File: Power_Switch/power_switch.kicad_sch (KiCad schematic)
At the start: 3 parts, among them J1 Conn_01x02_Pin, J2 Conn_01x02_Socket, SW1 SW_SPDT

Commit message: small changes - probably wont use
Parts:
- added H1, H2, H3: MountingHole, MountingHole:MountingHole_2.7mm_M2.5, symbol Mechanical:MountingHole
- added TP1, TP2: TestPoint, TestPoint:TestPoint_Pad_D1.5mm, symbol Connector:TestPoint
- J1, J2: footprint Connector_JST:JST_SH_BM02B-SRSS-TB_1x02-1MP_P1.00mm_Vertical -> Connector_JST:JST_SH_SM02B-SRSS-TB_1x02-1MP_P1.00mm_Horizontal
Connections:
- net V_BAT_SWITCHED: now reaches SW1.1 (A)
- net V_BAT_SWITCHED: now also J2.1 (Pin_1)
- net V_BAT: now reaches J1.1 (Pin_1), SW1.2 (B)
- net V_BAT: now also TP1.1
- net at SW1.3 (C): no longer J2.1 (Pin_1)
- net GND: now reaches J1.2 (Pin_2), J2.2 (Pin_2)
- net GND: now also TP2.1

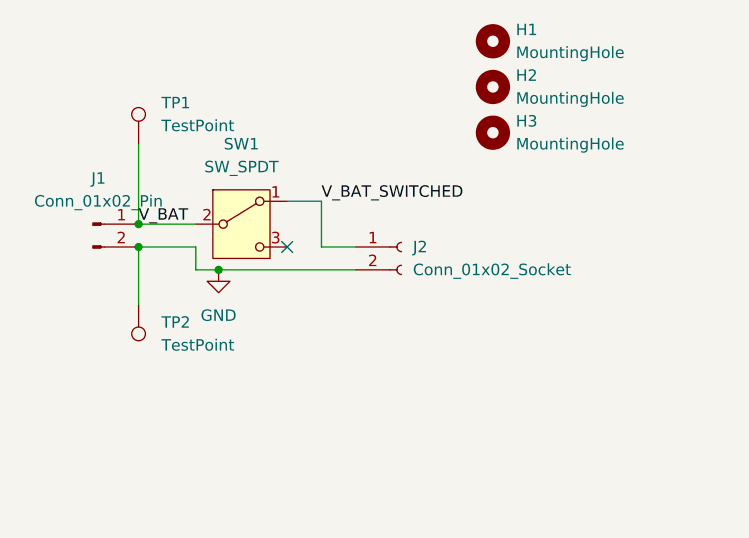
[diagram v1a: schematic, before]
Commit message: Switch_LED_daughter_board done
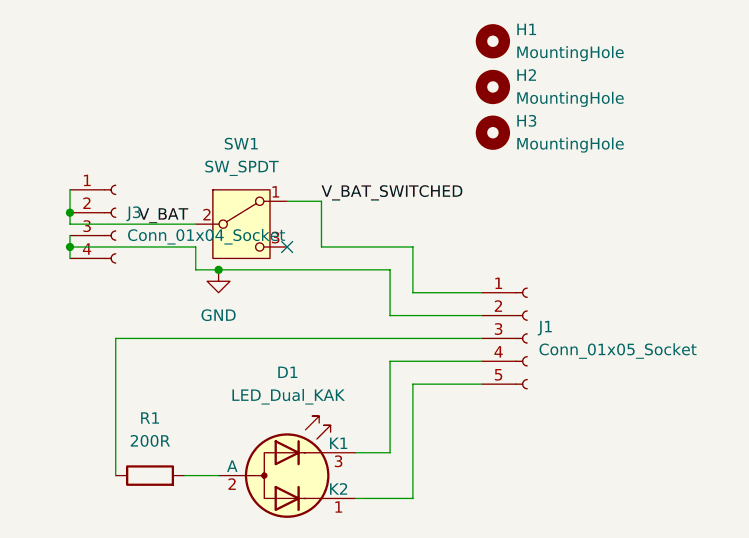
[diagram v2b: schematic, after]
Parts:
- removed J1: Conn_01x02_Pin, Connector_JST:JST_SH_SM02B-SRSS-TB_1x02-1MP_P1.00mm_Horizontal, symbol Connector:Conn_01x02_Pin
- removed J2: Conn_01x02_Socket, Connector_JST:JST_SH_SM02B-SRSS-TB_1x02-1MP_P1.00mm_Horizontal, symbol Connector:Conn_01x02_Socket
- removed TP1, TP2: TestPoint, TestPoint:TestPoint_Pad_D1.5mm, symbol Connector:TestPoint
- added D1: LED_Dual_KAK, JohnDeereLibrary:LED_Wurth_WL-SBSW, symbol Device:LED_Dual_KAK
- added J1: Conn_01x05_Socket, JohnDeereLibrary:5_pad_connector, symbol Connector:Conn_01x05_Socket
- added J3: Conn_01x04_Socket, JohnDeereLibrary:4_pad_connector, symbol Connector:Conn_01x04_Socket
- added R1: 200R, Resistor_SMD:R_0603_1608Metric, symbol Device:R
- SW1: footprint JohnDeereLibrary:ET01M3D1SAPE -> JohnDeereLibrary:ET01MD1CBE
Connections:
- net GND: now also J1.2 (Pin_2), J3.3 (Pin_3), J3.4 (Pin_4)
- net V_BAT: now also J3.1 (Pin_1), J3.2 (Pin_2)
- net V_BAT_SWITCHED: now also J1.1 (Pin_1)
- new net: J1.3 (Pin_3), R1.1
- new net: D1.2 (A), R1.2
- new net: D1.3 (K1), J1.4 (Pin_4)
- new net: D1.1 (K2), J1.5 (Pin_5)

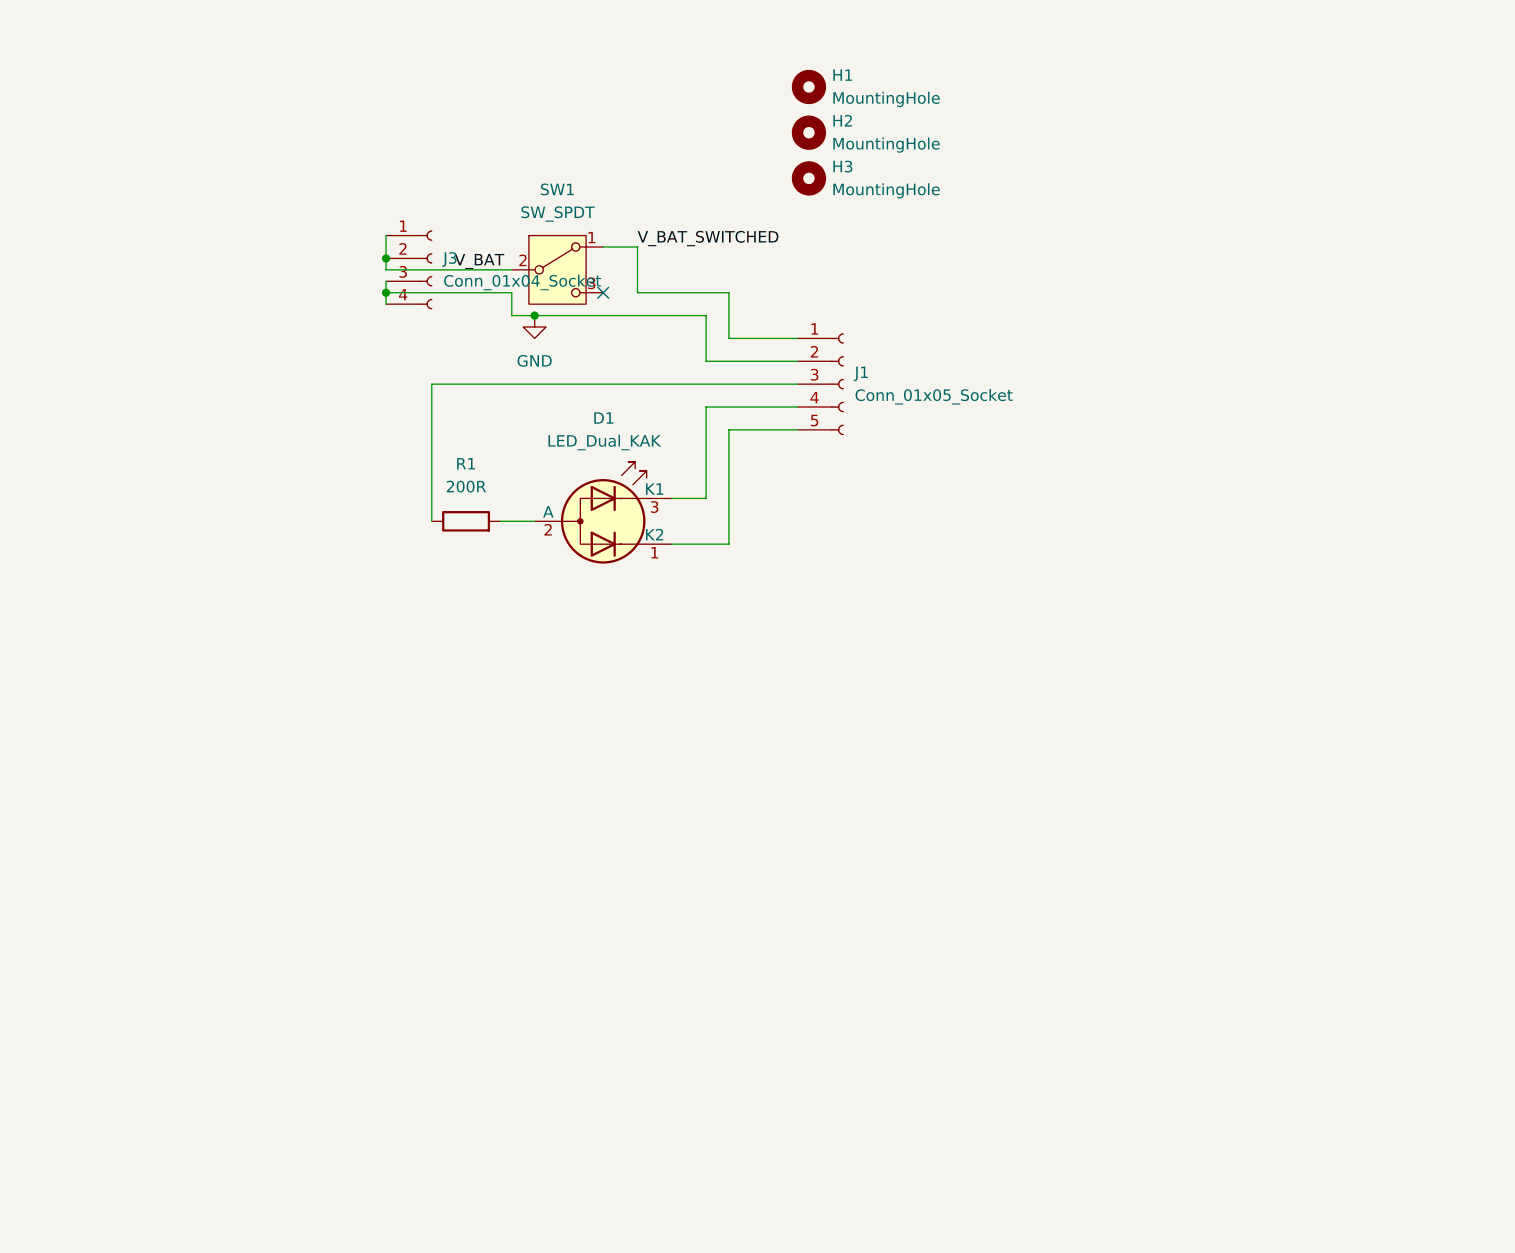
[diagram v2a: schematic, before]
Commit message: small changes to UX for charging
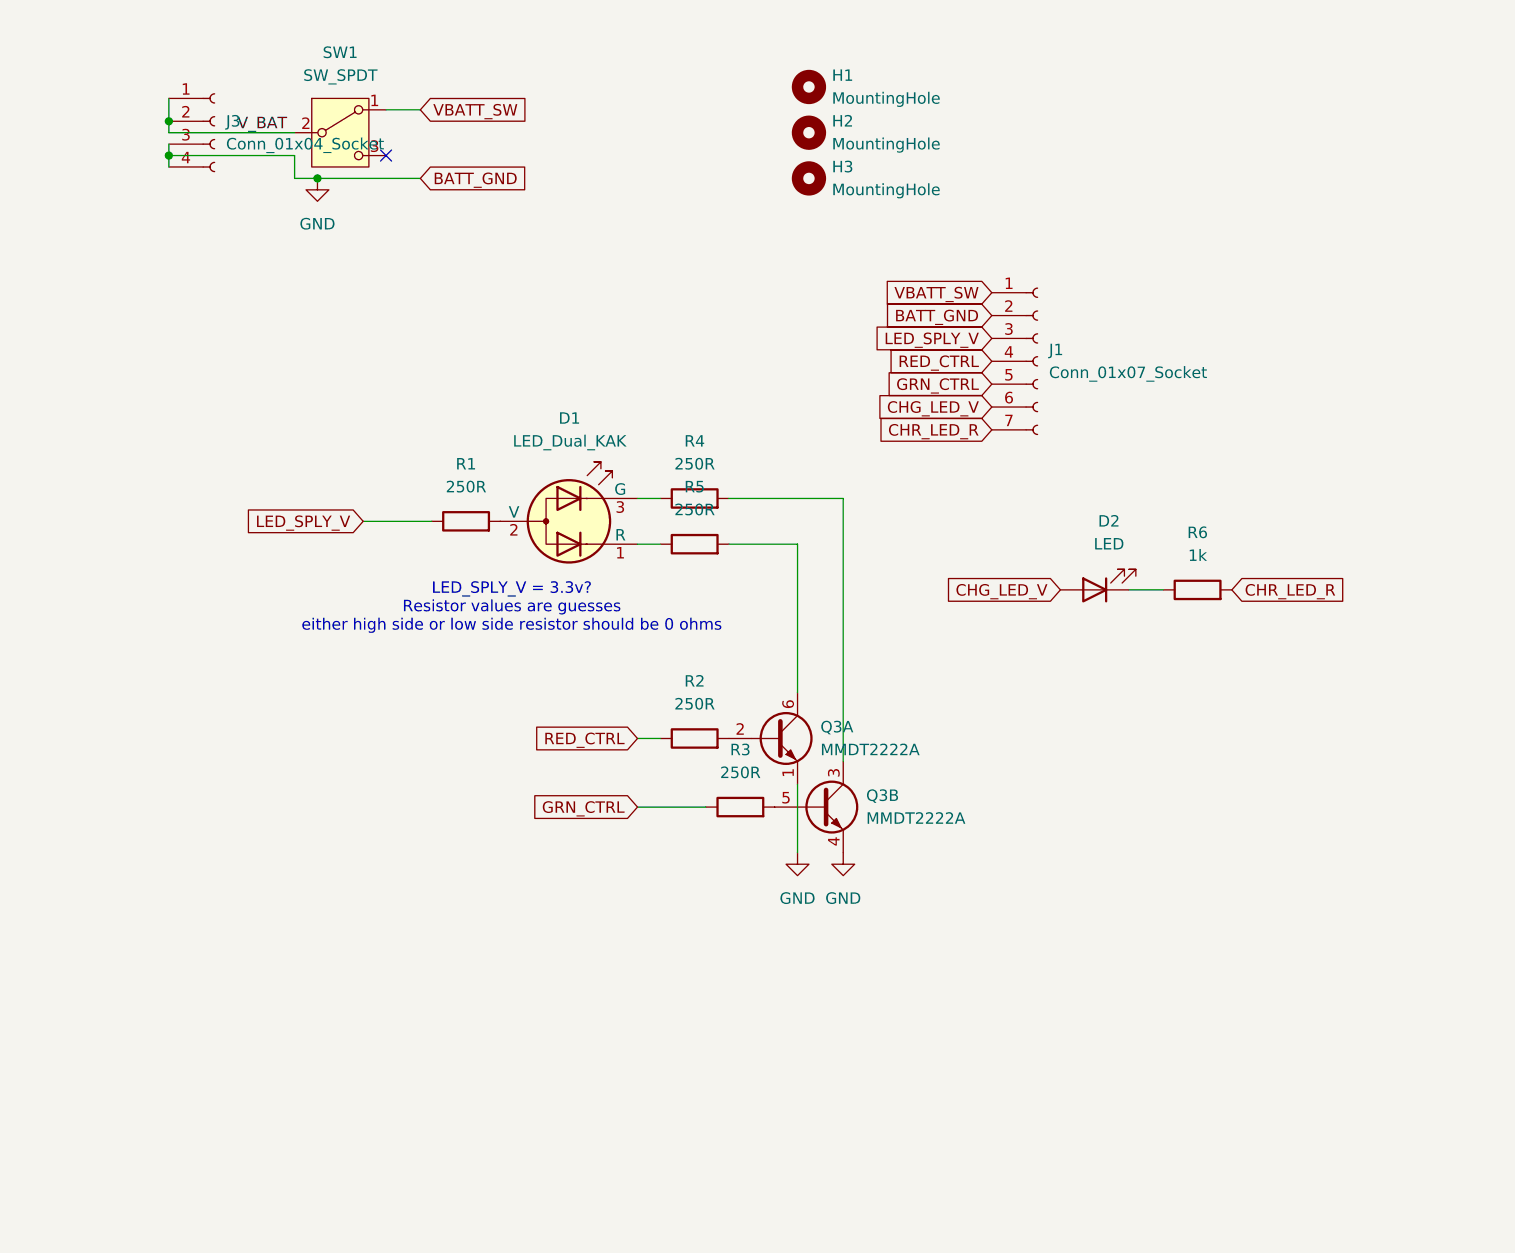
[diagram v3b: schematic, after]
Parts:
- removed J1: Conn_01x05_Socket, JohnDeereLibrary:5_pad_connector, symbol Connector:Conn_01x05_Socket
- added D2: LED, JohnDeereLibrary:LED_WURTH_155060AS75300, symbol Device:LED
- added J1: Conn_01x07_Socket, JohnDeereLibrary:7_pad_connector, symbol Connector:Conn_01x07_Socket
- added Q3: MMDT2222A, Package_TO_SOT_SMD:SOT-363_SC-70-6, symbol Transistor_BJT:MMDT2222A
- added R2, R3, R4, R5: 250R, Resistor_SMD:R_0603_1608Metric, symbol Device:R
- added R6: 1k, Resistor_SMD:R_0603_1608Metric, symbol Device:R
- R1: value 200R -> 250R
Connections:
- net GND: now also J1.2 (Pin_2), Q3.1 (E1), Q3.4 (E2)
- net LED_SPLY_V: now reaches R1.1
- net LED_SPLY_V: now also J1.3 (Pin_3)
- net at D1.3 (G): now also R4.1
- net at D1.1 (R): now also R5.1
- net V_BAT_SWITCHED renamed VBATT_SW
- net VBATT_SW: now also J1.1 (Pin_1)
- new net: Q3.2 (B1), R2.2
- new net: Q3.6 (C1), R5.2
- new net: D2.1 (K), R6.1
- new net: Q3.3 (C2), R4.2
- new net: Q3.5 (B2), R3.2
- new net CHG_LED_V: D2.2 (A), J1.6 (Pin_6)
- new net CHR_LED_R: J1.7 (Pin_7), R6.2
- new net GRN_CTRL: J1.5 (Pin_5), R3.1
- new net RED_CTRL: J1.4 (Pin_4), R2.1
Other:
- note added: "LED_SPLY_V = 3.3v? Resistor values are guesses either high side or low side resistor should be 0 ohms"
- moved on the sheet: D1, J3, SW1

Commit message: Finished Switch PCB - Almost done with Keyboard (Need to fix 3v3 and GND)
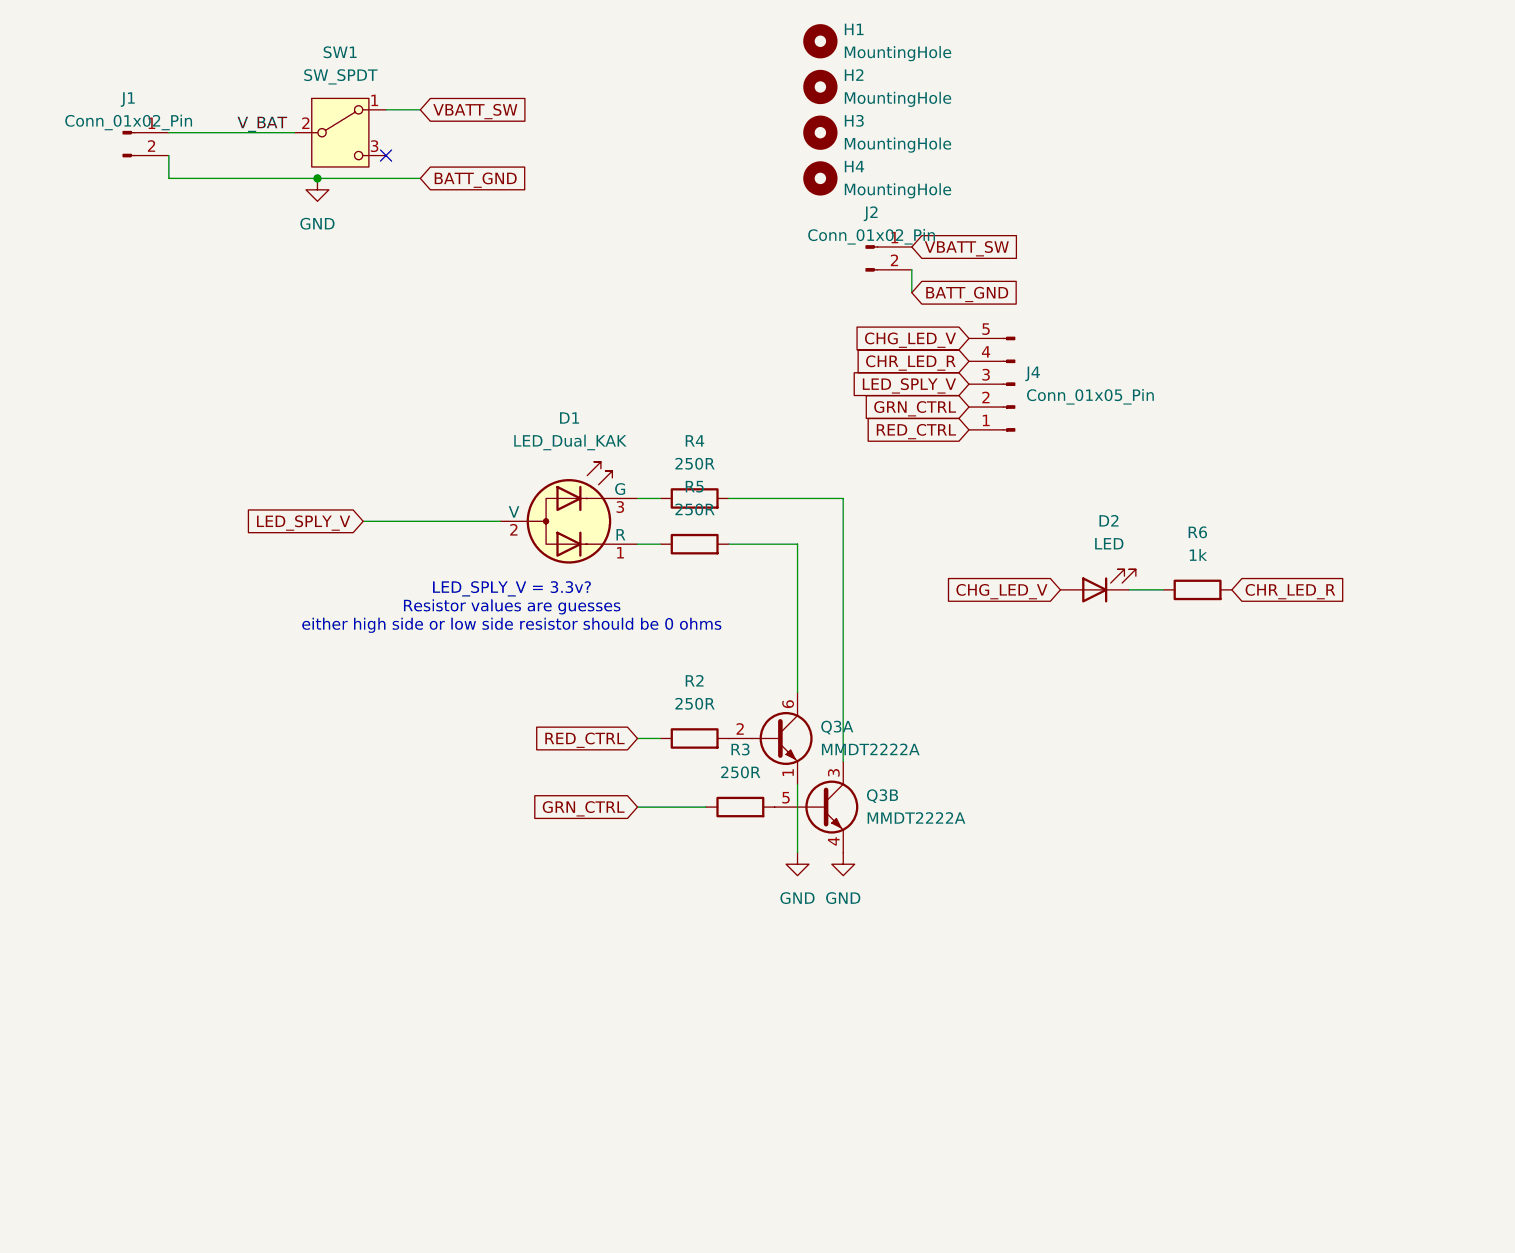
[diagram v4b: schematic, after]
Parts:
- removed J1: Conn_01x07_Socket, JohnDeereLibrary:7_pad_connector, symbol Connector:Conn_01x07_Socket
- removed J3: Conn_01x04_Socket, JohnDeereLibrary:4_pad_connector, symbol Connector:Conn_01x04_Socket
- removed R1: 250R, Resistor_SMD:R_0603_1608Metric, symbol Device:R
- added H4: MountingHole, MountingHole:MountingHole_2.7mm_M2.5, symbol Mechanical:MountingHole
- added J1, J2: Conn_01x02_Pin, JohnDeereLibrary:2_pad_connector, symbol Connector:Conn_01x02_Pin
- added J4: Conn_01x05_Pin, JohnDeereLibrary:5_pad_connector, symbol Connector:Conn_01x05_Pin
- R2, R3, R4, R5, R6: footprint Resistor_SMD:R_0603_1608Metric -> Resistor_SMD:R_0402_1005Metric
- SW1: footprint JohnDeereLibrary:ET01MD1CBE -> JohnDeereLibrary:ET01M3D1SAPE
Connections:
- net CHG_LED_V: now also J4.5 (Pin_5)
- net CHR_LED_R: now also J4.4 (Pin_4)
- net GND: now also J1.2 (Pin_2), J2.2 (Pin_2)
- net GRN_CTRL: now also J4.2 (Pin_2)
- net LED_SPLY_V: now also D1.2 (V), J4.3 (Pin_3)
- net RED_CTRL: now also J4.1 (Pin_1)
- net VBATT_SW: now also J2.1 (Pin_1)
- net V_BAT: now also J1.1 (Pin_1)
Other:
- moved on the sheet: H1, H2, H3

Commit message: small changes to led
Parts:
- removed D1: LED_Dual_KAK, JohnDeereLibrary:LED_Wurth_WL-SBSW, symbol Device:LED_Dual_KAK
- removed D2: LED, JohnDeereLibrary:LED_WURTH_155060AS75300, symbol Device:LED
- removed H3, H4: MountingHole, MountingHole:MountingHole_2.7mm_M2.5, symbol Mechanical:MountingHole
- removed J4: Conn_01x05_Pin, JohnDeereLibrary:5_pad_connector, symbol Connector:Conn_01x05_Pin
- removed Q3: MMDT2222A, Package_TO_SOT_SMD:SOT-363_SC-70-6, symbol Transistor_BJT:MMDT2222A
- removed R2, R3, R4, R5: 250R, Resistor_SMD:R_0402_1005Metric, symbol Device:R
- removed R6: 1k, Resistor_SMD:R_0402_1005Metric, symbol Device:R
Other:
- note removed: "LED_SPLY_V = 3.3v? Resistor values are guesses either high side or low side resistor should be 0 ohms"

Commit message: Power switch done
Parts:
- removed J1, J2: Conn_01x02_Pin, JohnDeereLibrary:2_pad_connector, symbol Connector:Conn_01x02_Pin
- added H3, H4: MountingHole, MountingHole:MountingHole_2.2mm_M2_ISO14580, symbol Mechanical:MountingHole
- added J1: Conn_01x03_Pin, Connector_Molex:Molex_Pico-EZmate_78171-0003_1x03-1MP_P1.20mm_Vertical, symbol Connector:Conn_01x03_Pin
- H1: footprint MountingHole:MountingHole_2.7mm_M2.5 -> MountingHole:MountingHole_2.2mm_M2_ISO14580
- H2: footprint MountingHole:MountingHole_2.7mm_M2.5 -> MountingHole:MountingHole_2.2mm_M2_ISO14580_Pad_TopBottom; symbol Mechanical:MountingHole -> Mechanical:MountingHole_Pad
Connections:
- net GND: now also H2.1, SW1.3 (C), J1.3 (Pin_3)
- net VBATT_SW renamed +BATT
- net +BATT: now also J1.1 (Pin_1)
- net V_BAT: no longer names the net of SW1.2 (B)
- net V_BAT: now also J1.2 (Pin_2)
- no-connect marks 1 -> 0

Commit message: Orginizing and small work done
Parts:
- added C10, C12: 4.7uF, Capacitor_SMD:C_0402_1005Metric, symbol Device:C
- added C11: 1uF, Capacitor_SMD:C_0402_1005Metric, symbol Device:C
- added D85: LED, JohnDeereLibrary:LED_WURTH_155060AS75300, symbol Device:LED
- added J2: FFC2B28-06-G, GCT:GCT_FFC2B28-06-G, symbol FFC2B28-06-G:FFC2B28-06-G
- added J6: Conn_01x02_Pin, Connector_PinSocket_2.54mm:PinSocket_1x02_P2.54mm_Vertical, symbol Connector:Conn_01x02_Pin
- added Q9: 2N7002, Package_TO_SOT_SMD:SOT-23, symbol Transistor_FET:2N7002
- added R10, R8, R9: 100k, Resistor_SMD:R_0402_1005Metric, symbol Device:R
- added R103: 1.87k, Resistor_SMD:R_0402_1005Metric, symbol Device:R
- added R104: TBD, Resistor_SMD:R_0402_1005Metric, symbol Device:R
- added R105: 47k, Resistor_SMD:R_0402_1005Metric, symbol Device:R
- added R106, R108: 10k, Resistor_SMD:R_0402_1005Metric, symbol Device:R
- added R107: 100R, Resistor_SMD:R_0402_1005Metric, symbol Device:R
- added R12: 1.5k, Resistor_SMD:R_0402_1005Metric, symbol Device:R
- added U6: BQ24075RGT, Package_DFN_QFN:VQFN-16-1EP_3x3mm_P0.5mm_EP1.6x1.6mm, symbol Battery_Management:BQ24075RGT
- SW1: footprint JohnDeereLibrary:ET01M3D1SAPE -> JohnDeereLibrary:ET01MD1CBE
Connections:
- net +BATT is gone; now on net GND: J1.1 (Pin_1), SW1.1 (A)
- net GND: now also C10.2, C11.2, C12.2, J2.2, J6.1 (Pin_1), Q9.2 (S), R10.2, R103.2, R104.2, R105.2, R106.2, R108.2, U6.17 (VSS), U6.4 (~{CE}), U6.5 (EN2), U6.8 (VSS); no longer J1.3 (Pin_3), SW1.3 (C)
- net SYSOFF: now reaches SW1.2 (B)
- net SYSOFF: now also Q9.3 (D), U6.15 (SYSOFF); no longer J1.2 (Pin_2)
- new net: R8.2, SW1.3 (C)
- new net: R104.1, U6.16 (ISET)
- new net: Q9.1 (G), R107.1, R108.1
- new net: R105.1, U6.14 (TMR)
- new net: D85.1 (K), R12.1
- new net: R12.2, U6.9 (~{CHG})
- new net: R103.1, U6.12 (ILIM)
- new net PGOOD: J2.3, U6.7 (~{PGOOD})
- new net TS: J1.2 (Pin_2), R106.1, U6.1 (TS)
- new net VBAT: R9.1
- new net VBATT: C12.1, J1.3 (Pin_3), J6.2 (Pin_2), R8.1, U6.2 (BAT), U6.3 (BAT)
- new net VBUS: C11.1, J2.5, R107.2, U6.13 (IN)
- new net VDIV: J2.1, R10.1, R9.2
- new net V_Raw: C10.1, D85.2 (A), J2.6, U6.10 (OUT), U6.11 (OUT), U6.6 (EN1)
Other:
- moved on the sheet: J1, SW1

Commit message: Work done
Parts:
- removed J2: FFC2B28-06-G, GCT:GCT_FFC2B28-06-G, symbol FFC2B28-06-G:FFC2B28-06-G
- added J2: GCT_FFC2B28-12-G, GCT:GCT_FFC2B28-12-G, symbol GCT:FFC2B28-12-G
- C10, C12: footprint Capacitor_SMD:C_0402_1005Metric -> Capacitor_SMD:C_0805_2012Metric
- C11: footprint Capacitor_SMD:C_0402_1005Metric -> Capacitor_SMD:C_1206_3216Metric
- R104: value TBD -> 1k
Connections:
- net GND: now also J2.10, J2.4, J2.5, J2.6, J2.9, J2.S1 (SHIELD), J2.S2 (SHIELD__1)
- net PGOOD: now also J2.8
- net VBAT: now also R8.1
- net VBATT: no longer R8.1
- net VBUS: now also J2.11, J2.12
- net VDIV: now also J2.7
- net V_Raw: now also J2.1, J2.2, J2.3
